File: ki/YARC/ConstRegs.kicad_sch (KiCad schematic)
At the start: 9 parts, among them U93 74LS32, U94 74HC245, U95 74HC245, U96 74LS32, U96A1 74LS32, U96B1 74LS32, U97 74HC00, U98 74HC245, U99 74HC245

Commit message: Condition and ALU control wiring complete.
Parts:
- renumbered U96A1 to U96, U96B1 to U96
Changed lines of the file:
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@@
   (symbol (lib_id "74xx:74LS32") (at 40.64 116.84 0) (unit 1)
     (in_bom yes) (on_board yes)
-    (property "Reference" "U96A1" (id 0) (at 45.72 111.76 0))
+    (property "Reference" "U96" (id 0) (at 45.72 111.76 0))
     (property "Value" "74LS32" (id 1) (at 40.64 116.84 0))
     (property "Footprint" "" (id 2) (at 40.64 116.84 0)
@@
   (symbol (lib_id "74xx:74LS32") (at 40.64 101.6 0) (unit 2)
     (in_bom yes) (on_board yes)
-    (property "Reference" "U96B1" (id 0) (at 45.72 96.52 0))
+    (property "Reference" "U96" (id 0) (at 45.72 96.52 0))
     (property "Value" "74LS32" (id 1) (at 40.64 101.6 0))
     (property "Footprint" "" (id 2) (at 40.64 101.6 0)

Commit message: Minor corrections to signal naming in memory controller
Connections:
- net ~{GR_RE} renamed ~{GR_EN}
- net ~{P2_RE} renamed grclk
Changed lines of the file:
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@@
     )
   )
-  (global_label "~{GR_RE}" (shape input) (at 33.02 119.38 180) (fields_autoplaced)
+  (global_label "~{GR_EN}" (shape input) (at 33.02 119.38 180) (fields_autoplaced)
     (effects (font (size 1.27 1.27)) (justify right))
-    (property "Intersheet References" "${INTERSHEET_REFS}" (id 0) (at 24.6802 119.3006 0)
+    (property "Intersheet References" "${INTERSHEET_REFS}" (id 0) (at 24.6198 119.3006 0)
       (effects (font (size 1.27 1.27)) (justify right) hide)
     )
   )
-  (global_label "~{P2_RE}" (shape input) (at 48.26 116.84 0) (fields_autoplaced)
+  (global_label "grclk" (shape input) (at 48.26 116.84 0) (fields_autoplaced)
     (effects (font (size 1.27 1.27)) (justify left))
-    (property "Intersheet References" "${INTERSHEET_REFS}" (id 0) (at 56.5393 116.7606 0)
+    (property "Intersheet References" "${INTERSHEET_REFS}" (id 0) (at 55.3902 116.7606 0)
       (effects (font (size 1.27 1.27)) (justify left) hide)
     )

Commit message: Implement ir0_en microcode bit to fix design error with JMP
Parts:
- removed unit 2 of U97
- removed unit 1 of U97
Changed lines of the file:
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@@
   (junction (at 251.46 83.82) (diameter 0) (color 0 0 0 0)
   )
-  (junction (at 187.96 162.56) (diameter 0) (color 0 0 0 0)
-  )
-  (junction (at 180.34 167.64) (diameter 0) (color 0 0 0 0)
-  )
   (junction (at 220.98 45.72) (diameter 0) (color 0 0 0 0)
   )
@@
   (junction (at 220.98 43.18) (diameter 0) (color 0 0 0 0)
   )
-  (junction (at 187.96 167.64) (diameter 0) (color 0 0 0 0)
-  )
   (junction (at 220.98 91.44) (diameter 0) (color 0 0 0 0)
   )
-  (junction (at 180.34 152.4) (diameter 0) (color 0 0 0 0)
-  )
   (junction (at 213.36 167.64) (diameter 0) (color 0 0 0 0)
   )
@@
     (stroke (width 0) (type default) (color 0 0 0 0))
   )
-  (wire (pts (xy 187.96 167.64) (xy 213.36 167.64))
-    (stroke (width 0) (type default) (color 0 0 0 0))
-  )
   (bus (pts (xy 88.9 30.48) (xy 88.9 48.26))
     (stroke (width 0) (type default) (color 0 0 0 0))
@@
     (stroke (width 0) (type default) (color 0 0 0 0))
   )
-  (wire (pts (xy 187.96 157.48) (xy 187.96 162.56))
-    (stroke (width 0) (type default) (color 0 0 0 0))
-  )
   (wire (pts (xy 220.98 96.52) (xy 220.98 93.98))
     (stroke (width 0) (type default) (color 0 0 0 0))
@@
     (stroke (width 0) (type default) (color 0 0 0 0))
   )
-  (wire (pts (xy 180.34 147.32) (xy 180.34 152.4))
-    (stroke (width 0) (type default) (color 0 0 0 0))
-  )
   (wire (pts (xy 109.22 114.3) (xy 111.76 114.3))
     (stroke (width 0) (type default) (color 0 0 0 0))
@@
     (stroke (width 0) (type default) (color 0 0 0 0))
   )
-  (wire (pts (xy 180.34 152.4) (xy 180.34 167.64))
-    (stroke (width 0) (type default) (color 0 0 0 0))
-  )
   (wire (pts (xy 193.04 63.5) (xy 190.5 63.5))
     (stroke (width 0) (type default) (color 0 0 0 0))
   )
-  (wire (pts (xy 187.96 162.56) (xy 187.96 167.64))
-    (stroke (width 0) (type default) (color 0 0 0 0))
-  )
-  (wire (pts (xy 180.34 167.64) (xy 187.96 167.64))
-    (stroke (width 0) (type default) (color 0 0 0 0))
-  )
   (wire (pts (xy 254 86.36) (xy 251.46 86.36))
     (stroke (width 0) (type default) (color 0 0 0 0))
@@
     (stroke (width 0) (type default) (color 0 0 0 0))
   )
-  (wire (pts (xy 160.02 167.64) (xy 180.34 167.64))
+  (wire (pts (xy 160.02 167.64) (xy 213.36 167.64))
     (stroke (width 0) (type default) (color 0 0 0 0))
   )
@@
     (pin "7")
   )
-  (symbol (lib_id "74xx:74HC00") (at 187.96 149.86 0) (unit 2)
-    (in_bom yes) (on_board yes)
-    (property "Reference" "U97" (id 0) (at 193.04 144.78 0))
-    (property "Value" "74HC00" (id 1) (at 187.96 149.86 0))
-    (property "Footprint" "" (id 2) (at 187.96 149.86 0)
-      (effects (font (size 1.27 1.27)) hide)
-    )
-    (property "Datasheet" "http://www.ti.com/lit/gpn/sn74hc00" (id 3) (at 187.96 149.86 0)
-      (effects (font (size 1.27 1.27)) hide)
-    )
-    (pin "4")
-    (pin "5")
-    (pin "6")
-  )
   (symbol (lib_id "74xx:74LS32") (at 182.88 63.5 0) (unit 3)
     (in_bom yes) (on_board yes)
@@
     (pin "7")
   )
-  (symbol (lib_id "74xx:74HC00") (at 195.58 160.02 0) (unit 1)
-    (in_bom yes) (on_board yes)
-    (property "Reference" "U97" (id 0) (at 200.66 154.94 0))
-    (property "Value" "74HC00" (id 1) (at 195.58 160.02 0))
-    (property "Footprint" "" (id 2) (at 195.58 160.02 0)
-      (effects (font (size 1.27 1.27)) hide)
-    )
-    (property "Datasheet" "http://www.ti.com/lit/gpn/sn74hc00" (id 3) (at 195.58 160.02 0)
-      (effects (font (size 1.27 1.27)) hide)
-    )
-    (pin "1")
-    (pin "2")
-    (pin "3")
-  )
   (symbol (lib_id "power:VCC") (at 251.46 22.86 0) (unit 1)

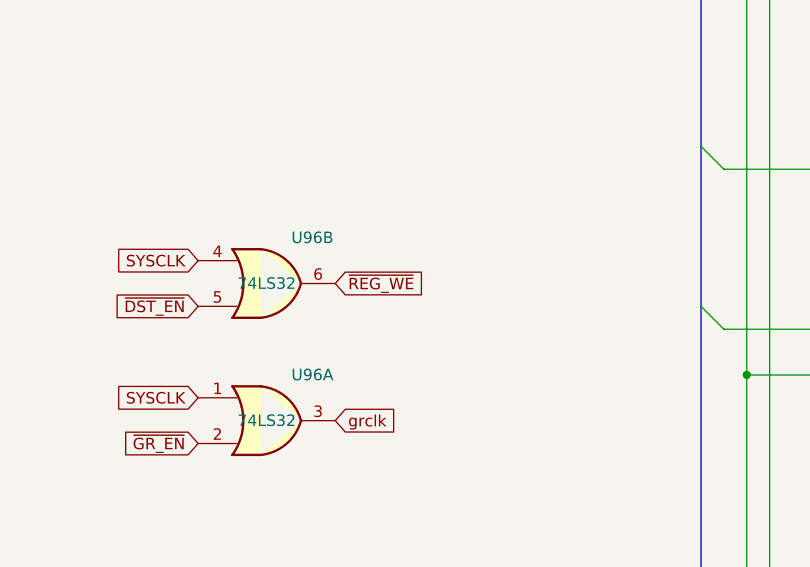
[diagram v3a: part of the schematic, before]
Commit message: Add delay line for general register write signal. Minor corrections and cleanups.
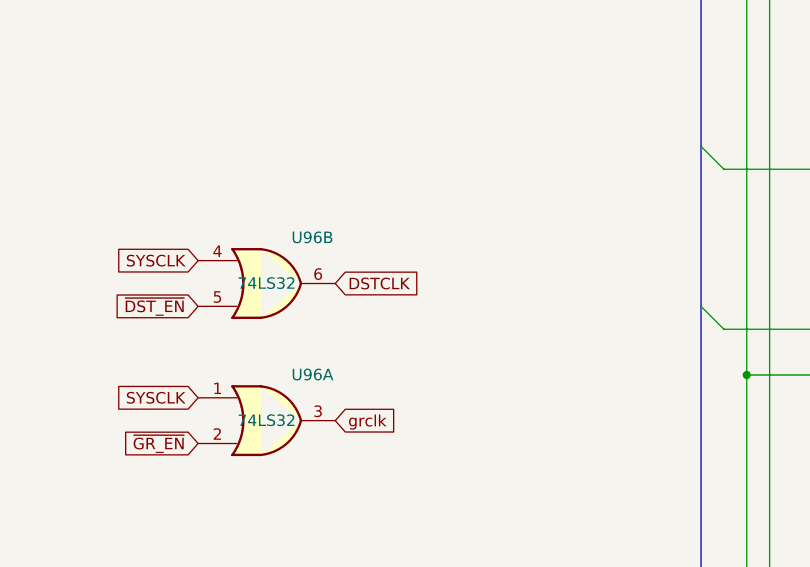
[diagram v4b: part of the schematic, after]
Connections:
- net ~{REG_WE} renamed DSTCLK
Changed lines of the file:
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@@
     (effects (font (size 1.27 1.27)) (justify right bottom))
   )
-  (global_label "~{REG_WE}" (shape input) (at 48.26 101.6 0) (fields_autoplaced)
+  (global_label "DSTCLK" (shape input) (at 48.26 101.6 0) (fields_autoplaced)
     (effects (font (size 1.27 1.27)) (justify left))
-    (property "Intersheet References" "${INTERSHEET_REFS}" (id 0) (at 57.9302 101.5206 0)
+    (property "Intersheet References" "${INTERSHEET_REFS}" (id 0) (at 57.6883 101.5206 0)
       (effects (font (size 1.27 1.27)) (justify left) hide)
     )

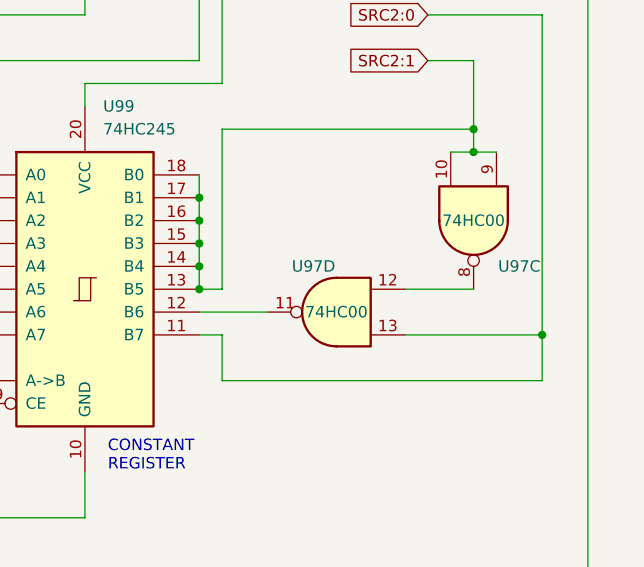
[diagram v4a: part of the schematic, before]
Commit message: Convert schematic to KiCad 7
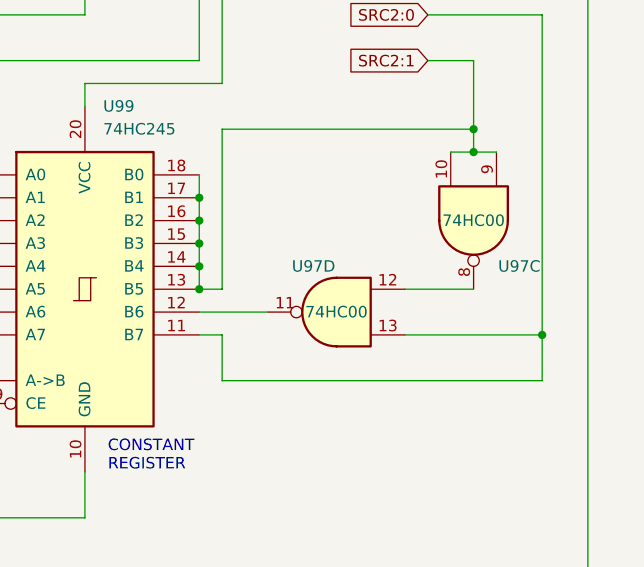
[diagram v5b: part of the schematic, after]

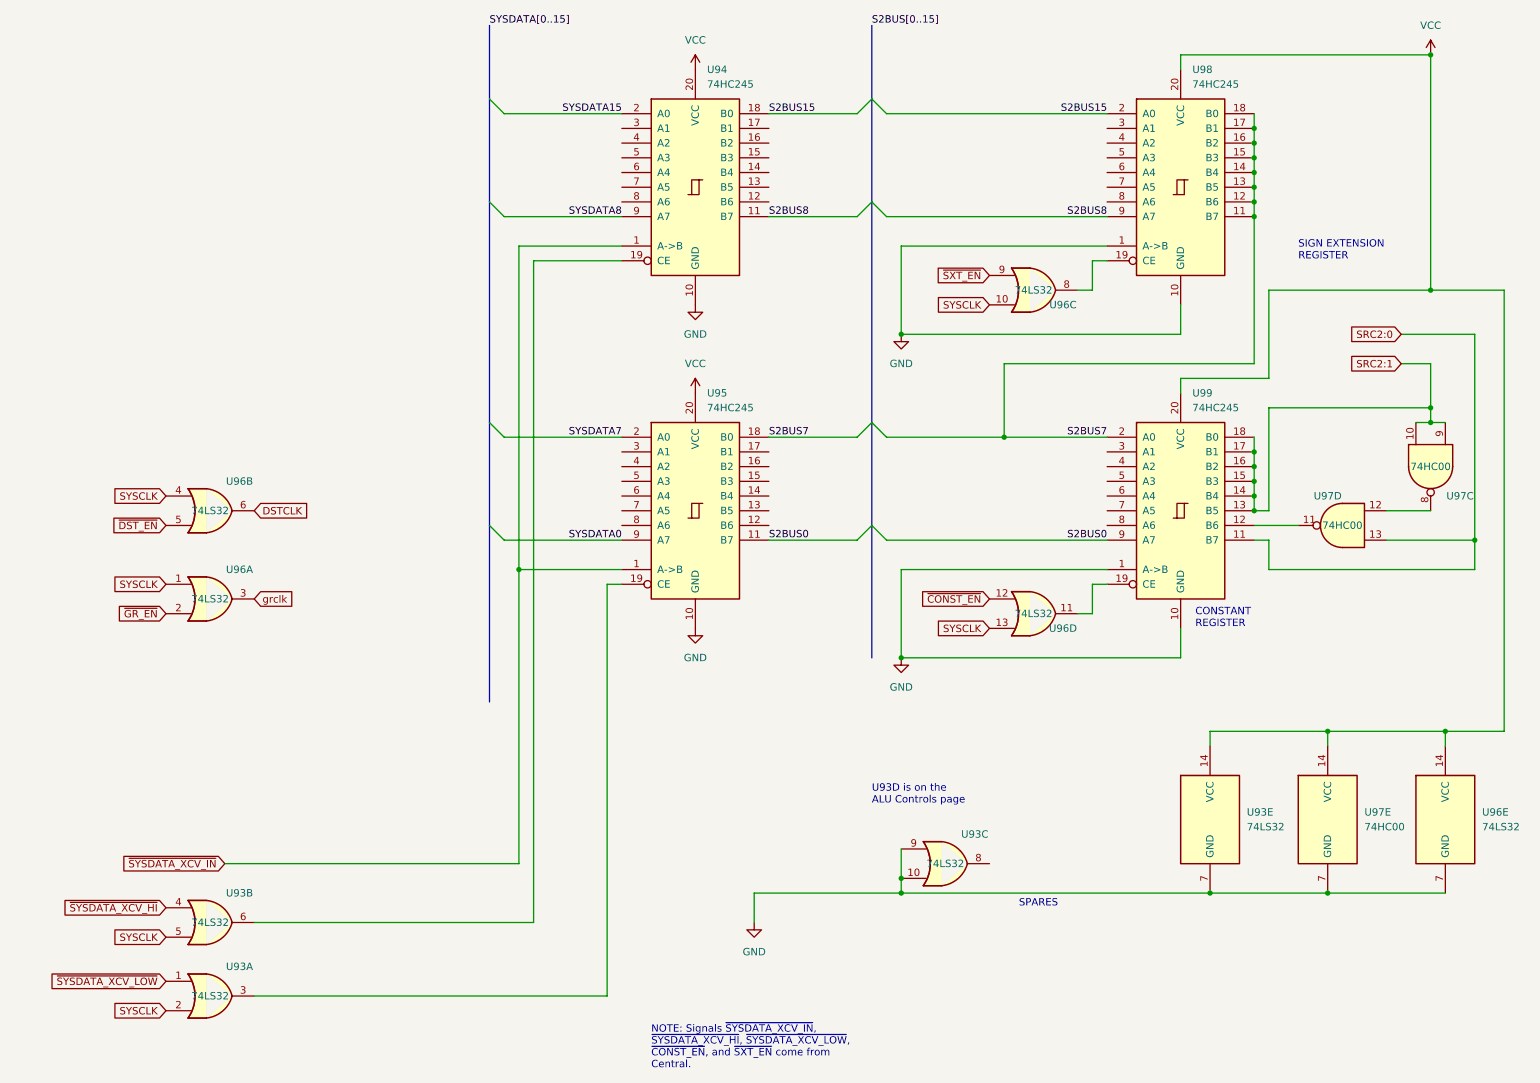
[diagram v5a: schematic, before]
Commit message: Ongoing fixes for ERC errors
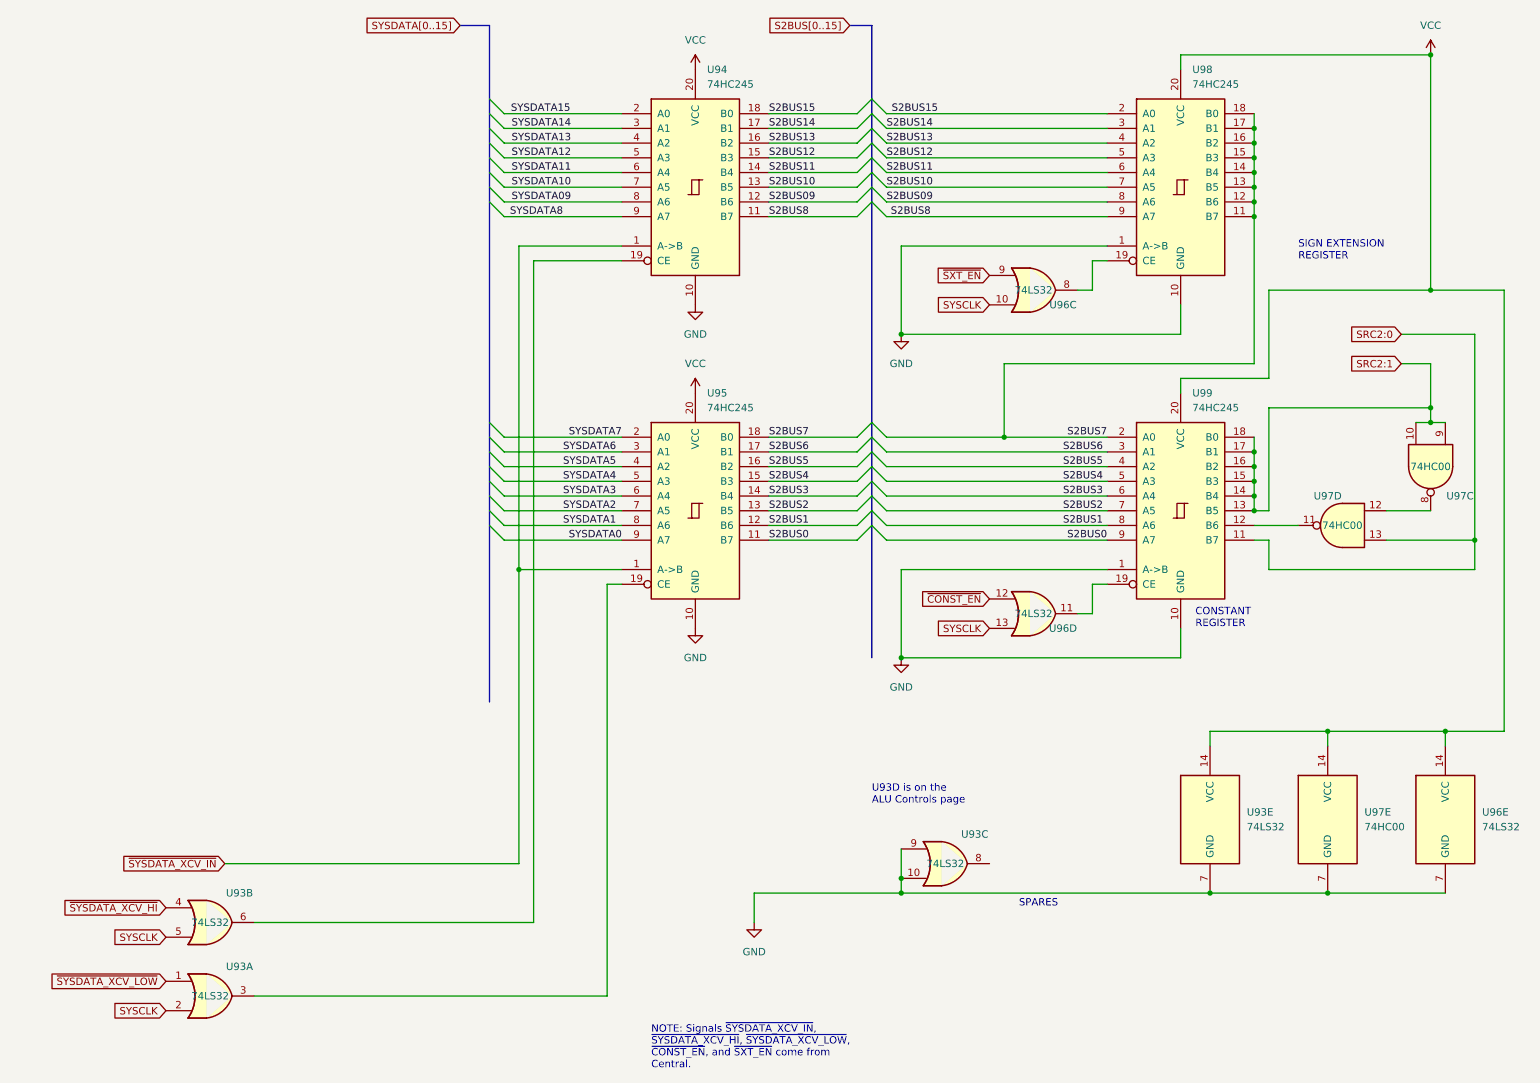
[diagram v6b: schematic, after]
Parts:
- removed unit 1 of U96
- removed unit 2 of U96
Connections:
- net S2BUS09: now reaches U94.12 (B6)
- net S2BUS09: now also U98.8 (A6)
- net S2BUS10: now reaches U94.13 (B5)
- net S2BUS10: now also U98.7 (A5)
- net S2BUS11: now reaches U94.14 (B4)
- net S2BUS11: now also U98.6 (A4)
- net S2BUS12: now reaches U94.15 (B3)
- net S2BUS12: now also U98.5 (A3)
- net S2BUS13: now reaches U94.16 (B2)
- net S2BUS13: now also U98.4 (A2)
- net S2BUS14: now reaches U94.17 (B1)
- net S2BUS14: now also U98.3 (A1)
- net SYSDATA14: now reaches U94.3 (A1)
- net SYSDATA13: now reaches U94.4 (A2)
- net SYSDATA12: now reaches U94.5 (A3)
- net SYSDATA11: now reaches U94.6 (A4)
- net SYSDATA10: now reaches U94.7 (A5)
- net SYSDATA09: now reaches U94.8 (A6)
- net S2BUS6: now reaches U99.3 (A1)
- net S2BUS6: now also U95.17 (B1)
- net S2BUS5: now reaches U99.4 (A2)
- net S2BUS5: now also U95.16 (B2)
- net S2BUS4: now reaches U99.5 (A3)
- net S2BUS4: now also U95.15 (B3)
- net S2BUS3: now reaches U99.6 (A4)
- net S2BUS3: now also U95.14 (B4)
- net S2BUS2: now reaches U99.7 (A5)
- net S2BUS2: now also U95.13 (B5)
- net S2BUS1: now reaches U99.8 (A6)
- net S2BUS1: now also U95.12 (B6)
- net SYSDATA6: now reaches U95.3 (A1)
- net SYSDATA5: now reaches U95.4 (A2)
- net SYSDATA4: now reaches U95.5 (A3)
- net SYSDATA3: now reaches U95.6 (A4)
- net SYSDATA2: now reaches U95.7 (A5)
- net SYSDATA1: now reaches U95.8 (A6)
